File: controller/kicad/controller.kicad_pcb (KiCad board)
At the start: 2 copper layers, 90 x 88.4 mm, 39 parts, among them J1 pcie_98, J2 USB_C_Receptacle_USB2.0, U1 WeAct_STM32H750_Module, U10 ESD5344D, U11 ESD5344D, U12 ESD5344D, U13 ESD5344D, U14 ESD5344D, U15 ESD5344D, U16 CP2102N-A02-GQFN28R, U17 ESD5344D, U2 ESD5344D, U3 ESD5344D, U4 ESD5344D, U5 ESD5344D, U6 ESD5344D, U7 ESD5344D, U8 ESD5344D, U9 ESD5344D

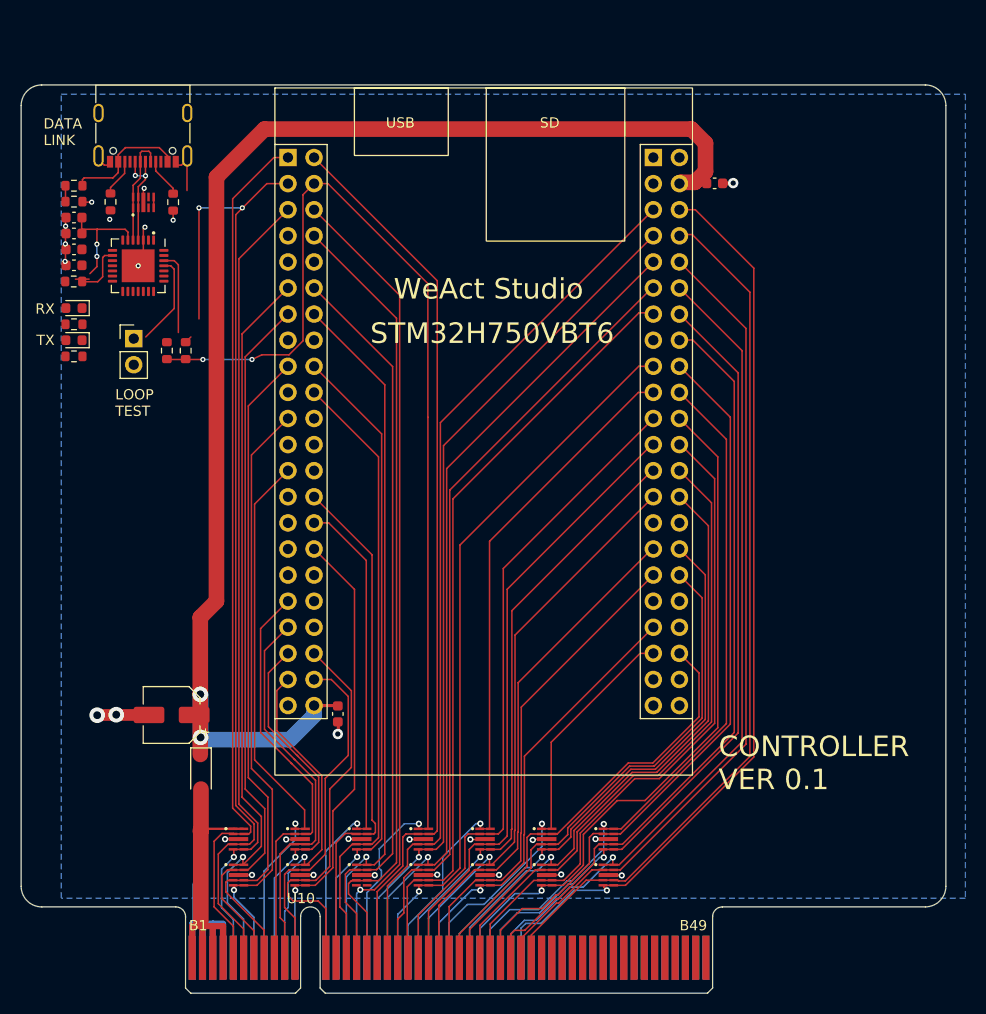
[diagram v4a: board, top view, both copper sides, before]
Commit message: Made the Controller PCB changes, per the schematic's TODOs.
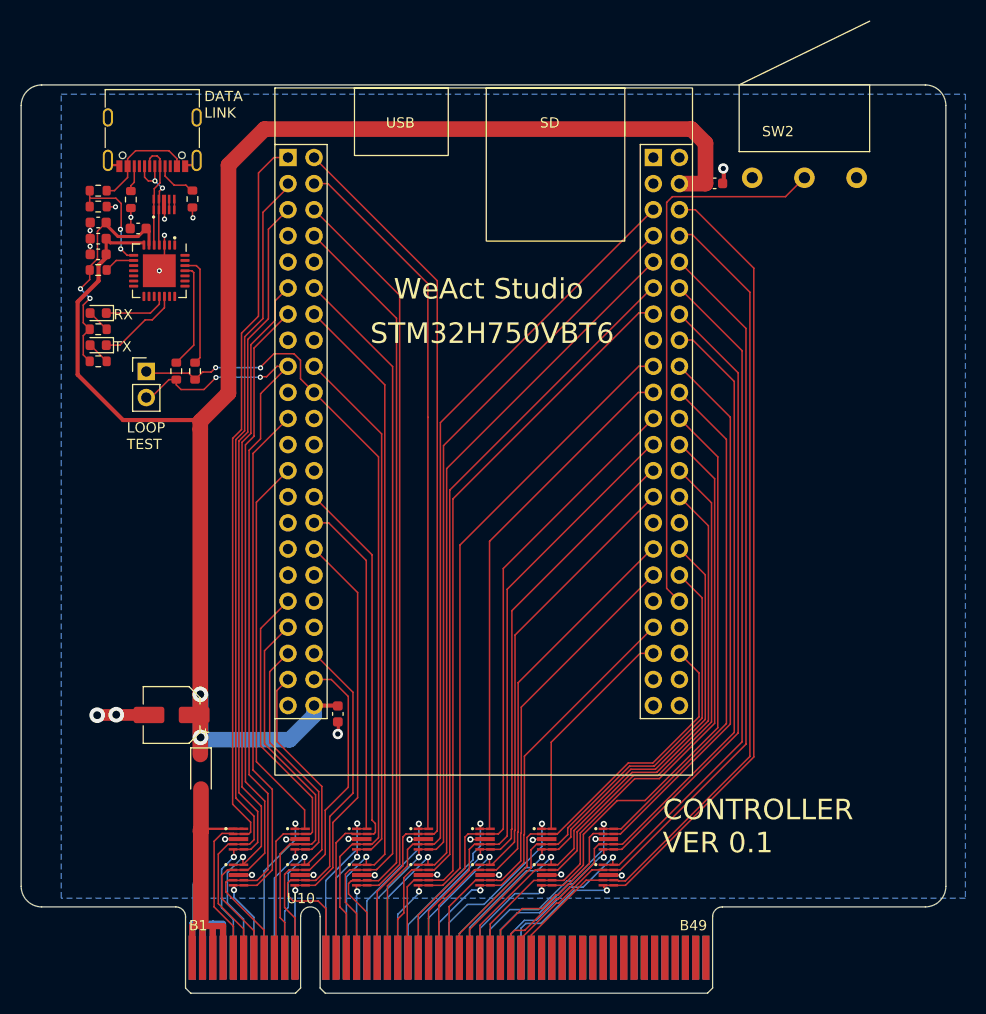
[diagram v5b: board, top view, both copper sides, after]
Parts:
- added SW2: SW_Push, controller:microswitch, F.Cu at (113.0, -19.4)
- moved C5 6.27 mm to (53.2, -14.4)
- moved C7 3.50 mm to (49.3, -13.4)
- moved JP1 3.42 mm to (54.0, -0.51)
- moved R5 2.63 mm to (49.3, -10.4)
- moved C6 2.41 mm to (49.3, -11.9)
- moved R7 2.41 mm to (49.3, -18.1)
- moved C8 2.41 mm to (49.3, -15.0)
- moved D2 2.41 mm to (49.3, -3.07)
- moved D3 2.41 mm to (49.3, -6.20)
- moved R8 2.41 mm to (49.3, -1.50)
- moved R9 2.41 mm to (49.3, -4.62)
- moved R6 2.41 mm to (49.3, -16.6)
- moved R3 2.19 mm to (56.9, -0.55)
- moved R4 2.19 mm to (58.8, -0.55)
- moved U16 2.11 mm to (55.3, -10.3)
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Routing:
- net /NRST: track 0.00 -> 53.7 mm
- net /+5V: track 132.4 -> 165.3 mm
- net /PB14: track 115.3 -> 84.7 mm, vias 3 -> 1
- net /PA10: track 60.6 -> 80.7 mm, vias 0 -> 2
- net /PB15: track 98.1 -> 81.9 mm, vias 2 -> 0
- net /PA9: track 64.9 -> 81.0 mm, vias 0 -> 2
- net Net-(U16-VDD): track 12.0 -> 23.0 mm
- net Net-(U16-VBUS): track 1.55 -> 10.7 mm, vias 0 -> 2
- net Net-(D2-K): track 0.00 -> 8.01 mm
- net Net-(D3-K): track 0.00 -> 6.57 mm
- net GND: track 61.7 -> 57.4 mm, vias 27 -> 26
- net Net-(U16-~{RSTb}): track 6.39 -> 3.01 mm
- net Net-(D3-A): track 0.00 -> 2.26 mm
- net Net-(D2-A): track 0.00 -> 2.26 mm
- net Net-(U16-TXD): track 8.89 -> 10.9 mm
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
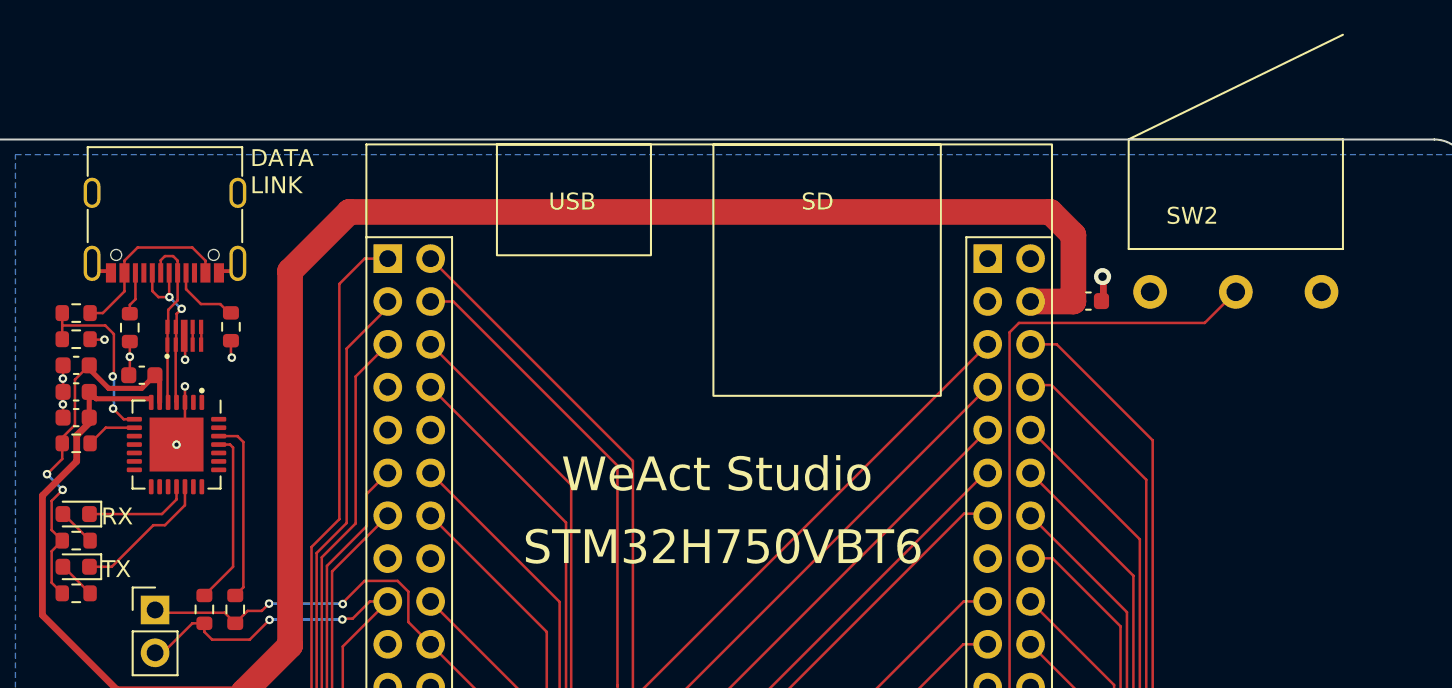
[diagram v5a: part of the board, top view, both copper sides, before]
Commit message: Verified and updated the microswitch footprint.
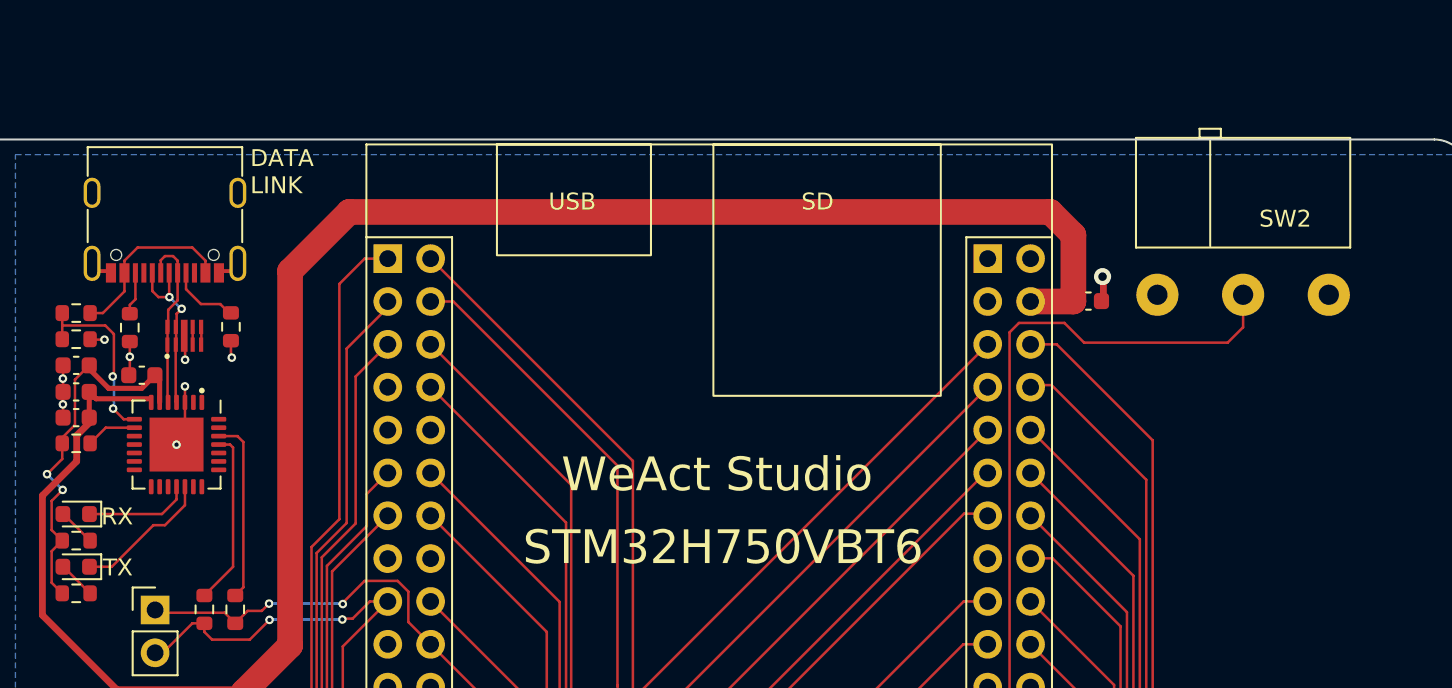
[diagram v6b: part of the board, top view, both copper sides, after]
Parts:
- SW2: value SW_Push -> D2F-01F-A
- moved SW2 5.51 mm to (118.5, -19.2)
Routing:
- net /NRST: track 53.7 -> 56.2 mm
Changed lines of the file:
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@@
         (effects (font (size 1 1) (thickness 0.15)))
     )
-    (fp_text user "USB" (at -9.525 -29.464 unlocked) (layer "F.SilkS")
+    (fp_text user "SD" (at 5.461 -29.464 unlocked) (layer "F.SilkS")
         (effects (font (size 1 1) (thickness 0.15)) (justify left bottom))
     )
-    (fp_text user "SD" (at 5.461 -29.464 unlocked) (layer "F.SilkS")
+    (fp_text user "USB" (at -9.525 -29.464 unlocked) (layer "F.SilkS")
         (effects (font (size 1 1) (thickness 0.15)) (justify left bottom))
     )
-    (fp_text user "${REFERENCE}" (at 17.78 0 90) (layer "F.Fab")
+    (fp_text user "${REFERENCE}" (at -17.78 0 90) (layer "F.Fab")
         (effects (font (size 1 1) (thickness 0.15)))
     )
-    (fp_text user "${REFERENCE}" (at -17.78 0 90) (layer "F.Fab")
+    (fp_text user "${REFERENCE}" (at 17.78 0 90) (layer "F.Fab")
         (effects (font (size 1 1) (thickness 0.15)))
     )
@@
         (effects (font (size 1 1) (thickness 0.15)) (justify left bottom mirror))
     )
-    (fp_text user "B1" (at -11.82 -6 unlocked) (layer "F.SilkS")
+    (fp_text user "B49" (at 35.93 -6 unlocked) (layer "F.SilkS")
         (effects (font (size 1 1) (thickness 0.15)) (justify left bottom))
     )
-    (fp_text user "B49" (at 35.93 -6 unlocked) (layer "F.SilkS")
+    (fp_text user "B1" (at -11.82 -6 unlocked) (layer "F.SilkS")
         (effects (font (size 1 1) (thickness 0.15)) (justify left bottom))
     )
@@
   )
   (footprint "controller:microswitch" (layer "F.Cu")
-    (at 113.0046 -19.3676)
+    (at 118.5164 -19.1954)
     (descr "E-Switch KS01Q01 http://spec_sheets.e-switch.com/specs/29-KS01Q01.pdf")
     (tags "Push Button")
@@
         (effects (font (size 1 1) (thickness 0.15)))
     )
-    (fp_text value "SW_Push" (at 2.5 9.5) (layer "F.Fab")
+    (fp_text value "D2F-01F-A\n" (at 2.5 9.5) (layer "F.Fab")
         (effects (font (size 1 1) (thickness 0.15)))
     )
@@
         (effects (font (size 1 1) (thickness 0.15)))
     )
-    (fp_line (start -1.27 -9.0424) (end -1.27 -2.54)
+    (fp_line (start -6.35 -9.3) (end -6.35 -2.8)
+      (stroke (width 0.12) (type default)) (layer "F.SilkS"))
+    (fp_line (start -6.35 -9.3) (end 6.35 -9.3)
+      (stroke (width 0.12) (type default)) (layer "F.SilkS"))
+    (fp_line (start -6.35 -2.8) (end 6.35 -2.8)
+      (stroke (width 0.12) (type default)) (layer "F.SilkS"))
+    (fp_line (start -2.5825 -9.84) (end -2.5825 -9.31)
+      (stroke (width 0.12) (type default)) (layer "F.SilkS"))
+    (fp_line (start -2.5825 -9.84) (end -1.3175 -9.84)
       (stroke (width 0.12) (type default)) (layer "F.SilkS"))
-    (fp_line (start -1.27 -9.0424) (end 11.43 -15.24)
+    (fp_line (start -2.5825 -9.31) (end -1.3175 -9.31)
       (stroke (width 0.12) (type default)) (layer "F.SilkS"))
-    (fp_line (start -1.27 -9.0424) (end 11.43 -9.0424)
+    (fp_line (start -1.95 -9.27) (end -1.95 -2.91)
       (stroke (width 0.12) (type default)) (layer "F.SilkS"))
-    (fp_line (start -1.27 -2.54) (end 11.43 -2.54)
+    (fp_line (start -1.3175 -9.31) (end -1.3175 -9.84)
       (stroke (width 0.12) (type default)) (layer "F.SilkS"))
-    (fp_line (start 11.43 -9.0424) (end 11.43 -2.54)
+    (fp_line (start 6.35 -9.3) (end 6.35 -2.8)
       (stroke (width 0.12) (type default)) (layer "F.SilkS"))
-    (pad "1" thru_hole circle (at 0 0) (size 2 2) (drill 1.1) (layers "*.Cu" "*.Mask")
+    (pad "" thru_hole circle (at 5.08 0) (size 2.5 2.5) (drill 1.2) (layers "*.Cu" "*.Mask"))
+    (pad "1" thru_hole circle (at -5.08 0) (size 2.5 2.5) (drill 1.2) (layers "*.Cu" "*.Mask")
       (net 1 "GND") (pinfunction "1") (pintype "passive"))
-    (pad "2" thru_hole circle (at 5.08 0) (size 2 2) (drill 1.1) (layers "*.Cu" "*.Mask")
+    (pad "2" thru_hole circle (at 0 0) (size 2.5 2.5) (drill 1.2) (layers "*.Cu" "*.Mask")
       (net 150 "/NRST") (pinfunction "2") (pintype "passive"))
-    (pad "3" thru_hole circle (at 10.16 0) (size 2 2) (drill 1.1) (layers "*.Cu" "*.Mask"))
     (model "${KIPRJMOD}/3d_models/Microswitch - Omron D2F-L-A.stp"
       (offset (xyz 5.08 5.715 2.921))
@@
     )
   )
-  (gr_text "TX" (at 50.8324 -2.3384) (layer "F.SilkS")
+  (gr_text "TX" (at 50.927 -2.4384) (layer "F.SilkS")
     (effects (font (size 1 1) (thickness 0.15)) (justify left bottom))
   )
@@
   (segment (start 48.5599 -6.1976) (end 48.5976 -6.1976) (width 0.1524) (layer "F.Cu") (net 142))
   (segment (start 48.5976 -6.1976) (end 50.1724 -4.6228) (width 0.1524) (layer "F.Cu") (net 142))
-  (segment (start 105.2322 -17.526) (end 116.243 -17.526) (width 0.1524) (layer "F.Cu") (net 150))
+  (segment (start 118.5164 -17.272) (end 118.5164 -19.1954) (width 0.1524) (layer "F.Cu") (net 150))
   (segment (start 104.6734 20.5994) (end 104.6734 -16.9672) (width 0.1524) (layer "F.Cu") (net 150))
-  (segment (start 116.243 -17.526) (end 118.0846 -19.3676) (width 0.1524) (layer "F.Cu") (net 150))
+  (segment (start 117.602 -16.3576) (end 118.5164 -17.272) (width 0.1524) (layer "F.Cu") (net 150))
+  (segment (start 107.9246 -17.526) (end 109.093 -16.3576) (width 0.1524) (layer "F.Cu") (net 150))
   (segment (start 104.6734 -16.9672) (end 105.2322 -17.526) (width 0.1524) (layer "F.Cu") (net 150))
   (segment (start 105.918 21.844) (end 104.6734 20.5994) (width 0.1524) (layer "F.Cu") (net 150))
+  (segment (start 105.2322 -17.526) (end 107.9246 -17.526) (width 0.1524) (layer "F.Cu") (net 150))
+  (segment (start 109.093 -16.3576) (end 117.602 -16.3576) (width 0.1524) (layer "F.Cu") (net 150))
   (segment (start 49.8349 -6.1976) (end 54.4322 -6.1976) (width 0.1524) (layer "F.Cu") (net 151))
   (segment (start 55.2958 -7.0612) (end 55.2958 -7.8169) (width 0.1524) (layer "F.Cu") (net 151))

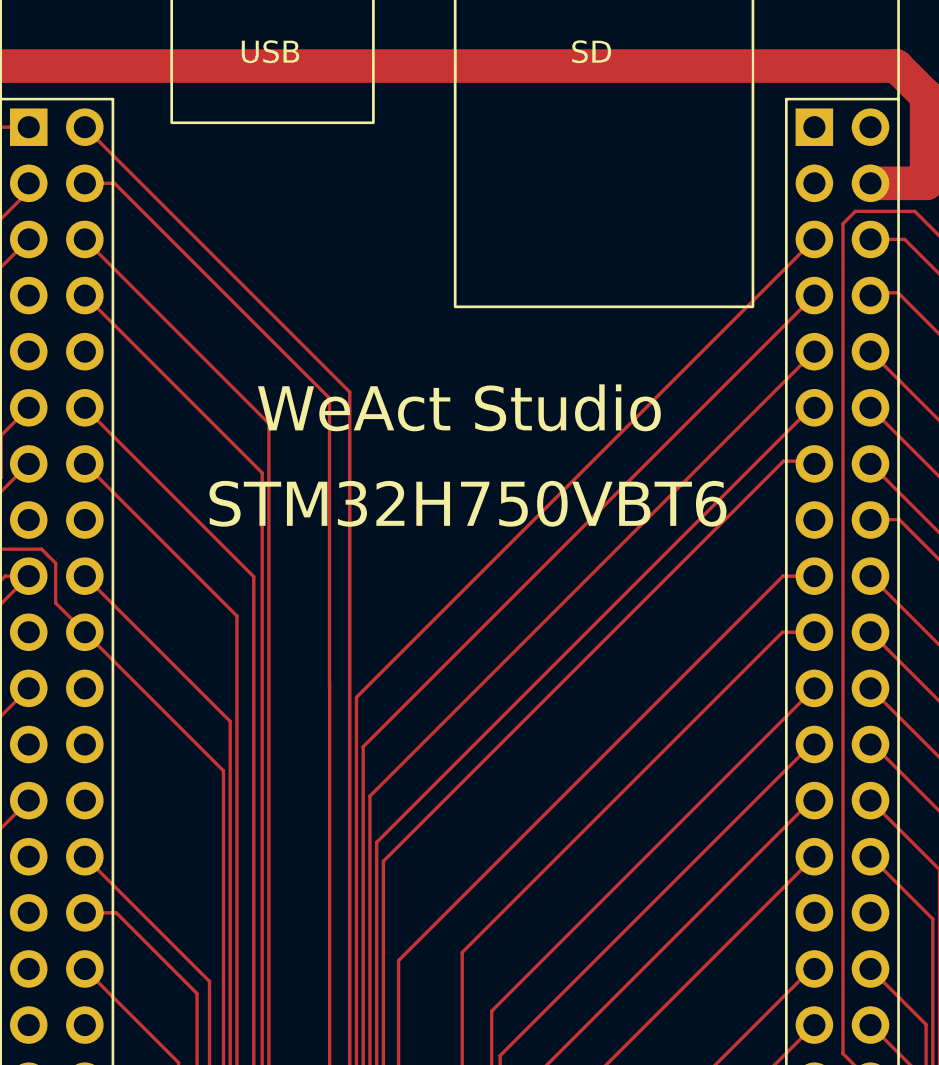
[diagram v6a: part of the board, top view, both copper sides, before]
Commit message: Added to the controller board text to remove D10.
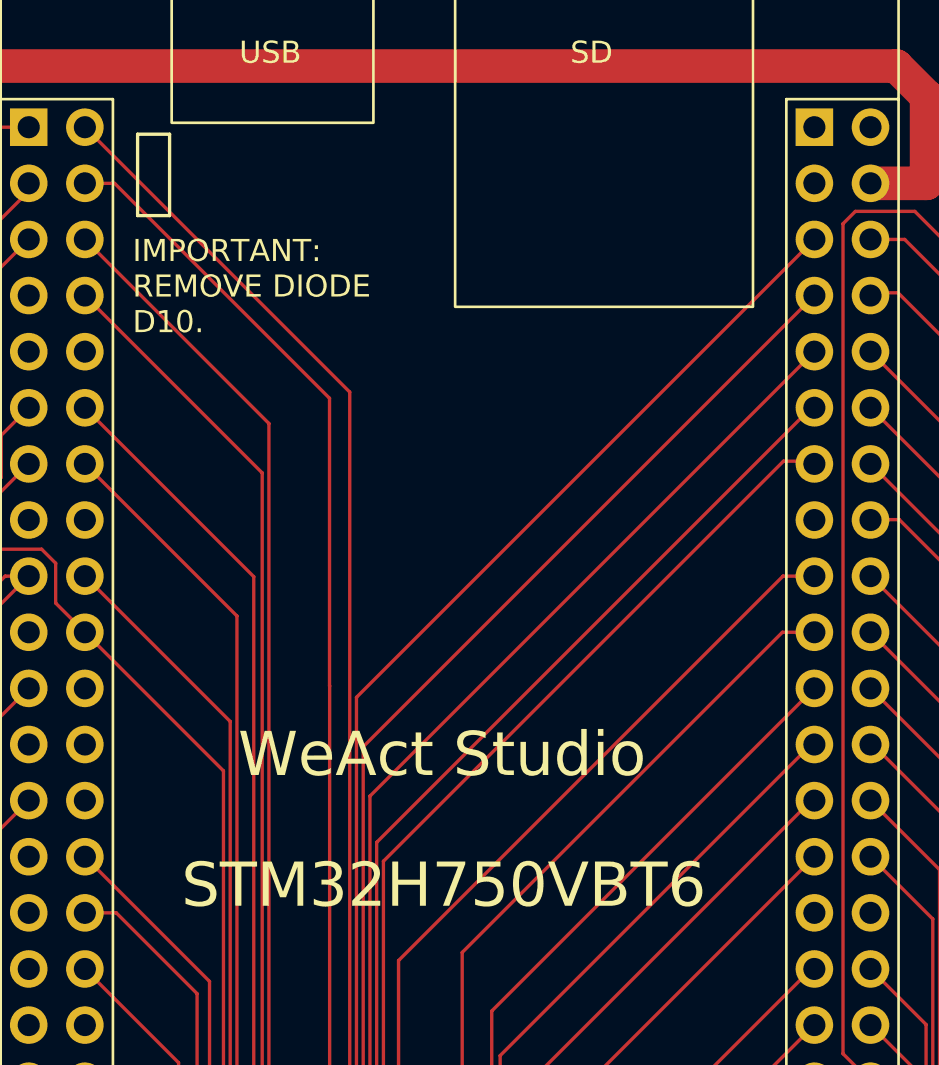
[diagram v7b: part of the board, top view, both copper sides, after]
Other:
- board text added: "IMPORTANT: REMOVE DIODE D10."
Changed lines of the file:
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@@
     )
   )
+  (gr_rect (start 72.7456 -21.0185) (end 74.1934 -17.3355)
+    (stroke (width 0.15) (type default)) (fill none) (layer "F.SilkS"))
   (gr_text "TX" (at 50.927 -2.4384) (layer "F.SilkS")
     (effects (font (size 1 1) (thickness 0.15)) (justify left bottom))
@@
     (effects (font (size 1 1) (thickness 0.15)) (justify left bottom))
   )
-  (gr_text "WeAct Studio" (at 78.105 -7.366) (layer "F.SilkS")
+  (gr_text "WeAct Studio" (at 77.2922 8.2296) (layer "F.SilkS")
     (effects (font (size 2 2) (thickness 0.3)) (justify left bottom))
   )
-  (gr_text "STM32H750VBT6" (at 75.819 -3.048) (layer "F.SilkS")
+  (gr_text "STM32H750VBT6" (at 74.7268 14.1478) (layer "F.SilkS")
     (effects (font (size 2 2) (thickness 0.3)) (justify left bottom))
   )
@@
     (effects (font (size 2 2) (thickness 0.2)) (justify left bottom))
   )
+  (gr_text "IMPORTANT: \nREMOVE DIODE\nD10." (at 72.517 -11.938) (layer "F.SilkS")
+    (effects (font (size 1 1) (thickness 0.15)) (justify left bottom))
+  )
   (gr_text "RX" (at 50.8324 -5.4626) (layer "F.SilkS")
